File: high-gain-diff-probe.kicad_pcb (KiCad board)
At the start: 4 copper layers, 110 x 80 mm, 107 parts, among them J1 30V DC IN, J2 BNC, J4 BNC, J5 BNC, K1 FTR-B3SA012Z, K2 FTR-B3SA012Z, Q1 MMBT3906, SW1 MB04L1NCGD, SW2 MB05L1NCGD, SW3 SPDT, SW4 MB04L1NCGD, SW6 SPDT, U1 AD8428BRZ, U2 OP1177AR, U3 BUF634A, U6 LM393, U7 AD8671, U8 BUF634A

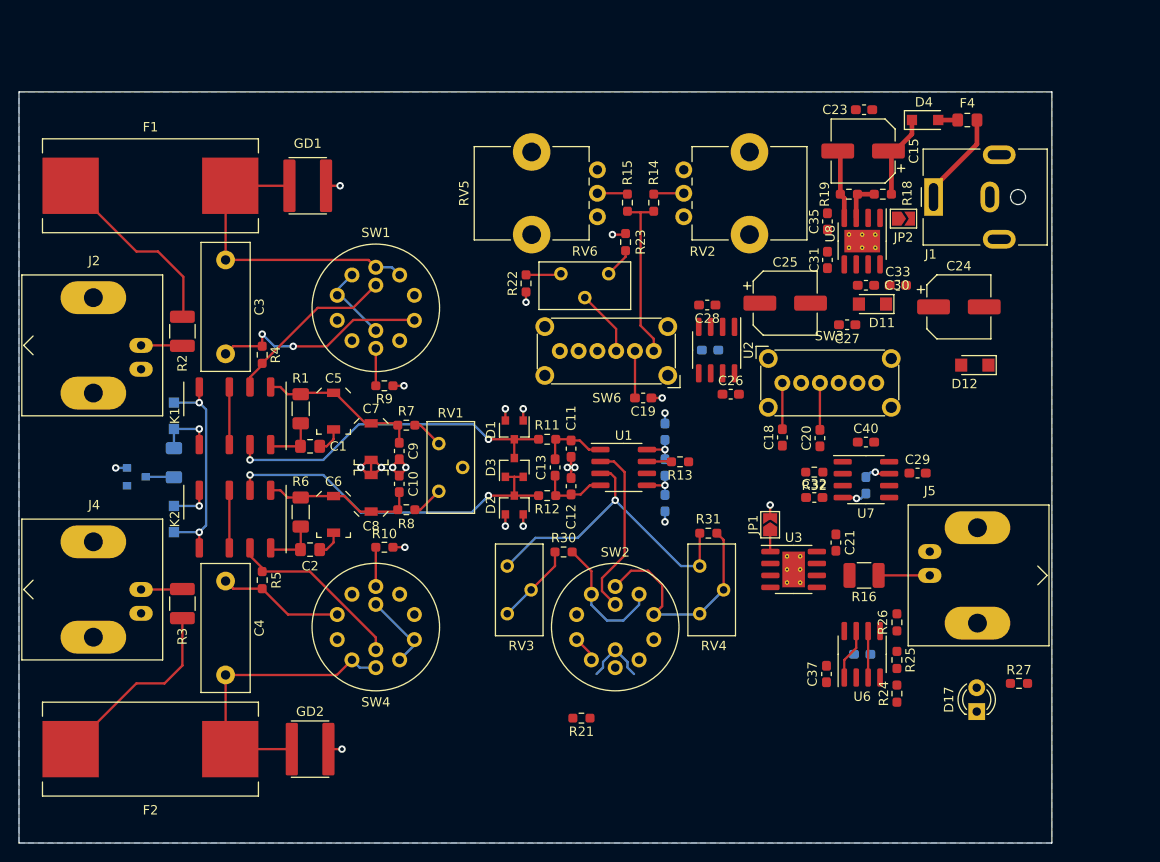
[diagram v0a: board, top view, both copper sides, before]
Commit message: Add 3D Models
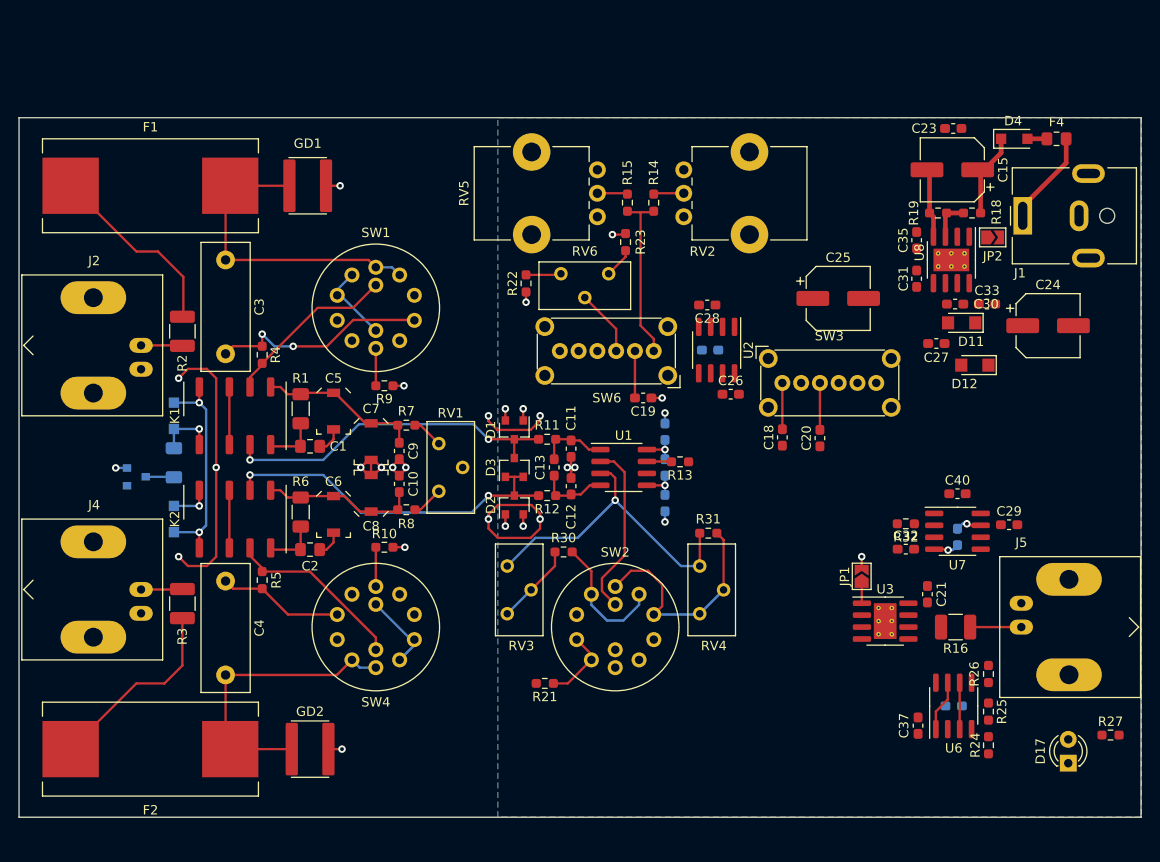
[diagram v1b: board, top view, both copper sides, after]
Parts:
- moved C21 11.2 mm to (186.8, 113.5)
- moved C29 11.2 mm to (195.4, 106.1)
- moved C32 11.2 mm to (184.4, 108.7)
- moved C34 11.2 mm to (189.6, 125.4)
- moved C37 11.2 mm to (185.8, 127.5)
- moved C38 11.2 mm to (189.9, 107.4)
- moved C40 11.2 mm to (189.9, 102.8)
- moved D17 11.2 mm to (201.8, 131.5)
- moved J5 11.2 mm to (196.8, 117.0)
- moved JP1 11.2 mm to (179.8, 111.6)
- moved R16 11.2 mm to (189.8, 117.0)
- moved R24 11.2 mm to (193.2, 129.6)
- moved R25 11.2 mm to (193.2, 126.0)
- moved R26 11.2 mm to (193.2, 122.0)
- moved R27 11.2 mm to (206.2, 128.5)
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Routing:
- net GND: track 30.2 -> 64.6 mm, vias 13 -> 18
- net (no net): track 0.00 -> 15.7 mm, vias 0 -> 2
- net Net-(R21-Pad1): track 3.34 -> 8.16 mm
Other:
- board size 110 x 80 mm -> 119.5 x 74.5 mm
- board text added: "Designed for Enclosure: Hammond Mfg 1455J1201"

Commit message: More layout
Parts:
- removed C38: 1uF, Capacitor_SMD:C_0603_1608Metric_Pad1.05x0.95mm_HandSolder
- C21, C26, C28, C29, C32, C33, C35, JP1: moved to B.Cu
- moved C35 48.5 mm to (181.0, 124.1), turned to 180 degrees
- moved C33 40.0 mm to (186.5, 122.1), turned to 270 degrees
- moved R24 31.7 mm to (188.5, 98.2), turned to 180 degrees
- moved D17 31.5 mm to (200.8, 100.0), turned to 0 degrees
- moved C37 30.3 mm to (197.2, 99.4), turned to 90 degrees
- moved C25 27.7 mm to (190.4, 57.6)
- moved R27 27.6 mm to (205.6, 100.9), turned to 270 degrees
- moved C24 27.3 mm to (201.2, 57.6)
- moved R25 25.6 mm to (189.4, 100.7), turned to 90 degrees
- moved C34 24.3 mm to (193.3, 101.4), turned to 180 degrees
- moved U6 24.3 mm to (193.3, 101.4), turned to 270 degrees
- moved C29 21.0 mm to (176.7, 115.6), turned to 180 degrees
- moved R26 19.4 mm to (188.5, 103.2), turned to 0 degrees
- moved R23 17.1 mm to (138.0, 80.1)
- moved SW6 17.0 mm to (174.5, 89.5)
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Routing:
- net Net-(C18-Pad1): track 0.00 -> 19.5 mm
- net -15V: track 23.8 -> 42.6 mm, vias 7 -> 10
- net Net-(R14-Pad1): track 18.2 -> 0.00 mm
- net Net-(C40-Pad2): track 0.00 -> 15.3 mm
- net /REF: track 0.00 -> 15.2 mm
- net /OUT: track 10.4 -> 25.2 mm
- net GND: track 64.6 -> 77.1 mm, vias 18 -> 25
- net +15V: track 21.0 -> 30.6 mm, vias 6 -> 10
- net Net-(R24-Pad1): track 0.00 -> 8.68 mm
- net Net-(RV6-Pad2): track 7.07 -> 0.00 mm
- net Net-(C37-Pad2): track 5.48 -> 12.4 mm
- net Net-(R16-Pad2): track 0.00 -> 5.41 mm
- net Net-(R18-Pad2): track 4.37 -> 0.00 mm
- net Net-(R25-Pad1): track 0.00 -> 4.26 mm
- net Net-(R22-Pad2): track 3.77 -> 0.00 mm
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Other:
- board text added: "Covered by extrusion slots"
- board text added: "Edge of Top Panel (estimate)"

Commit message: Finish Layout
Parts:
- C23: moved to B.Cu
- C3, C4: value 2.2uF 63V FILM -> 1uF 100V FILM; footprint Capacitor_THT:C_Rect_L13.5mm_W5.0mm_P10.00mm_FKS3_FKP3_MKS4 -> Capacitor_THT:C_Rect_L7.2mm_W7.2mm_P5.00mm_FKS2_FKP2_MKS2_MKP2
- Q1: moved to F.Cu
- moved Q1 51.9 mm to (145.5, 130.0), turned to 270 degrees
- moved R22 34.9 mm to (174.7, 96.9), turned to 270 degrees
- moved C24 30.5 mm to (181.0, 80.5), turned to 90 degrees
- moved RV6 30.4 mm to (166.0, 97.8), turned to 180 degrees
- moved R23 29.5 mm to (162.3, 96.9)
- moved C23 18.0 mm to (206.0, 71.2), turned to 270 degrees
- moved C25 16.2 mm to (181.0, 70.8), turned to 90 degrees
- moved C27 12.5 mm to (189.4, 74.4), turned to 0 degrees
- moved C31 11.5 mm to (186.3, 68.4)
- moved C30 10.8 mm to (186.3, 72.4), turned to 90 degrees
- moved SW6 10.0 mm to (164.5, 89.5), turned to 0 degrees
- moved R19 9.84 mm to (197.0, 69.2), turned to 90 degrees
- moved D12 9.28 mm to (190.0, 80.0), turned to 270 degrees
- moved R18 8.27 mm to (198.9, 69.2), turned to 270 degrees
- moved U8 7.53 mm to (191.5, 70.7), turned to 180 degrees
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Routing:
- net -15V: track 42.6 -> 146.0 mm, vias 10 -> 19
- net Net-(Q1-Pad3): track 3.02 -> 96.8 mm, vias 0 -> 1
- net GND: track 77.1 -> 148.9 mm, vias 25 -> 40
- net Net-(C18-Pad1): track 19.5 -> 40.8 mm
- net +15V: track 30.6 -> 51.4 mm, vias 10 -> 19
- net Net-(C19-Pad2): track 2.68 -> 18.1 mm
- net Net-(R14-Pad1): track 0.00 -> 15.3 mm
- net /OUT: track 25.2 -> 36.9 mm
- net Net-(F2-Pad2): track 20.6 -> 13.8 mm
- net Net-(F1-Pad2): track 20.3 -> 13.8 mm
- net Net-(RV6-Pad2): track 0.00 -> 5.76 mm
- net Net-(R18-Pad2): track 0.00 -> 4.94 mm
- net Net-(C4-Pad2): track 31.7 -> 27.0 mm
- net Net-(C3-Pad2): track 33.6 -> 29.2 mm
- net Net-(R22-Pad2): track 0.00 -> 3.67 mm
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- added copper zone on F.Cu, net -15V
- added copper zone on F.Cu, net GND

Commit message: Tweaks
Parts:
- moved R23 9.34 mm to (169.2, 103.2), turned to 0 degrees
- moved SW3 6.72 mm to (171.0, 112.0), turned to 270 degrees
- moved R22 6.31 mm to (174.3, 103.2), turned to 180 degrees
- moved C18 3.93 mm to (171.0, 107.2), turned to 270 degrees
- moved RV6 3.80 mm to (168.3, 100.8)
- moved SW6 3.04 mm to (164.0, 92.5)
- moved R14 1.80 mm to (159.0, 79.4)
- moved R15 1.80 mm to (157.0, 79.4)
- moved RV2 1.80 mm to (162.0, 81.0)
- moved RV5 1.80 mm to (154.0, 76.0)
- moved C20 1.50 mm to (176.0, 111.2), turned to 270 degrees
- moved C19 0.40 mm to (153.1, 85.4)
- moved R31 0.29 mm to (163.7, 107.0)
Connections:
- SW6 pad : (no net) -> GND
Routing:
- net GND: track 148.9 -> 153.8 mm
- net Net-(C18-Pad1): track 40.8 -> 37.0 mm
- net Net-(C19-Pad2): track 18.1 -> 20.8 mm
- net Net-(C20-Pad2): track 4.92 -> 6.63 mm
- net Net-(C18-Pad2): track 5.34 -> 3.92 mm
- net Net-(R22-Pad2): track 3.67 -> 2.40 mm
- net Net-(R23-Pad1): track 3.67 -> 2.41 mm
- net Net-(RV6-Pad2): track 5.76 -> 6.94 mm
- net Net-(R14-Pad1): track 15.3 -> 16.2 mm
- net /FIL+: track 34.7 -> 34.5 mm, vias 1 -> 2
